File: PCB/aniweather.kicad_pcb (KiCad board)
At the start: 2 copper layers, 55 x 75 mm, 26 parts, among them SW1 SW_DIP_x01, SW2 SW_Push, U5 TPS63001

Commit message: Reroute board
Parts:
- added R4: 100k, Resistor_THT:R_Axial_DIN0207_L6.3mm_D2.5mm_P10.16mm_Horizontal, F.Cu at (139.3, 136.2)
- added SW3: SW_Push, Button_Switch_THT:SW_PUSH_6mm, F.Cu at (122.0, 136.2)
- moved G1 71.2 mm to (69.2, 98.7)
- moved G2 71.2 mm to (69.2, 98.7)
- moved C1 6.21 mm to (122.8, 125.9), turned to 0 degrees
- moved SW2 0.45 mm to (158.4, 129.7)
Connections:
- U1 pad 10: SD_MISO -> MISO
- U1 pad 11: SD_SCK -> SCK
- U1 pad 5: SDA -> MOSI
- U1 pad 9: SD_MOSI -> MOSI
- U2 pad 0: SDA -> Net-(U2-A0)
- U2 pad 10: SD_CS -> CS_LCD
- U2 pad 2: RESET -> MISO
- U2 pad 3: CS_LCD -> RESET
- U2 pad 4: SCK -> unconnected-(U2-A4-Pad4)
- U2 pad 6: SD_SCK -> SCK
- U2 pad 7: SD_MISO -> MOSI
- U2 pad 8: SD_MOSI -> SD_CS
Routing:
- net MOSI: track 0.00 -> 62.5 mm
- net MISO: track 0.00 -> 46.1 mm
- net SCK: track 15.4 -> 60.4 mm
- net Net-(U2-A0): track 0.00 -> 41.7 mm
- net SD_MISO: track 25.3 -> 0.00 mm
- net SD_SCK: track 25.3 -> 0.00 mm
- net SD_MOSI: track 25.3 -> 0.00 mm
- net CS_LCD: track 12.9 -> 36.2 mm
- net SDA: track 14.7 -> 0.00 mm
- net +3.3V: track 89.2 -> 101.8 mm
- net GND: track 23.3 -> 19.9 mm, vias 72 -> 71
- net RESET: track 12.9 -> 11.1 mm
- net SD_CS: track 25.8 -> 26.7 mm

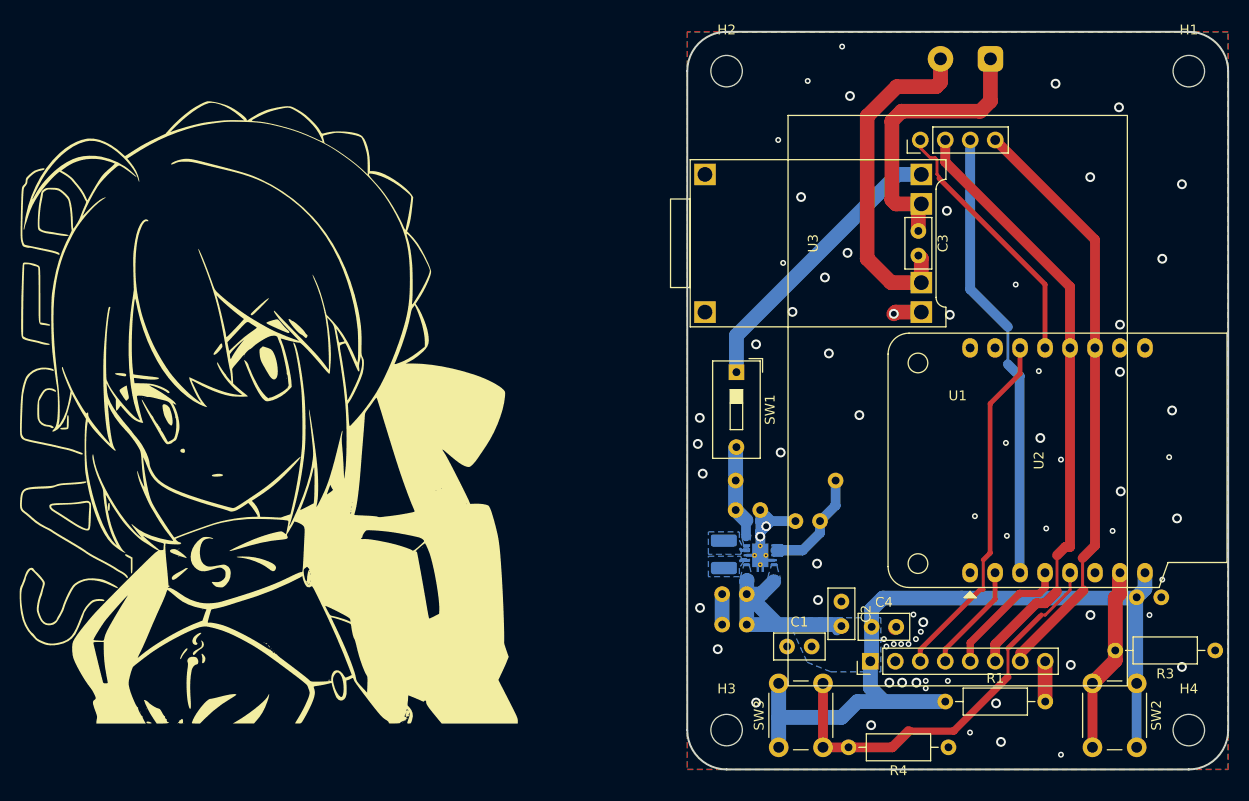
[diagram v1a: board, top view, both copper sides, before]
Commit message: Round corner cases and button holes
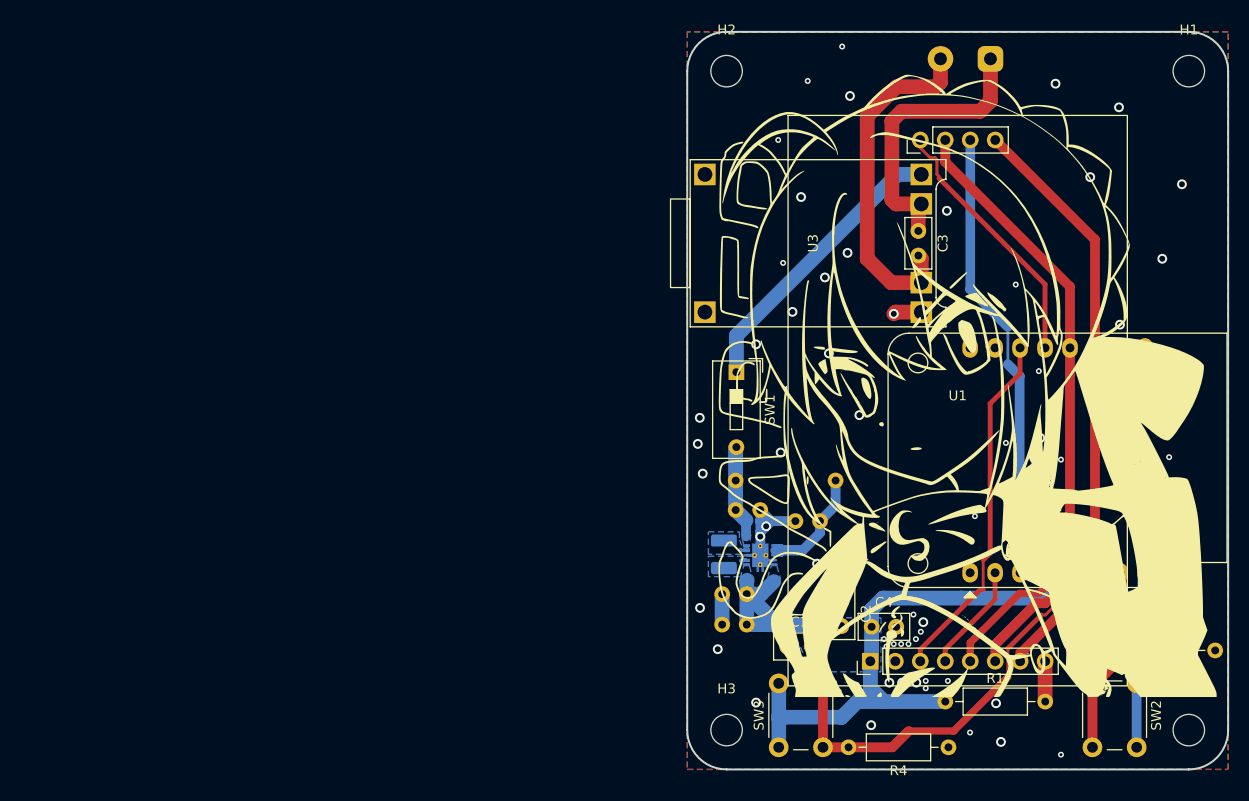
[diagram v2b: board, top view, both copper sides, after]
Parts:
- moved G1 71.1 mm to (140.3, 96.0)
- moved G2 71.1 mm to (140.3, 96.0)
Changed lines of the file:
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@@
 	(footprint "LOGO"
 		(layer "F.Cu")
-		(at 69.2 98.725)
+		(at 140.25115 96.027339)
 		(property "Reference" "G2"
 			(at 0 0 0)
@@
 		)
 		(property "Footprint" ""
-			(at 0 0 90)
+			(at 0 0 -90)
 			(layer "F.Fab")
 			(hide yes)
@@
 		(tags "C Disc series Radial pin pitch 2.50mm  diameter 5mm width 2.5mm Capacitor")
 		(property "Reference" "C1"
-			(at 1.25 -2.5 360)
+			(at 1.25 -2.5 0)
 			(layer "F.SilkS")
 			(effects
@@
 		)
 		(property "Value" "Tiny"
-			(at 1.25 2.5 360)
+			(at 1.25 2.5 0)
 			(layer "F.Fab")
 			(effects
@@
 		)
 		(property "Footprint" ""
-			(at 0 0 360)
+			(at 0 0 0)
 			(layer "F.Fab")
 			(hide yes)
@@
 		)
 		(fp_text user "${REFERENCE}"
-			(at 1.25 0 360)
+			(at 1.25 0 0)
 			(layer "F.Fab")
 			(effects
@@
 		(tags "Resistor Axial_DIN0207 series Axial Horizontal pin pitch 10.16mm 0.25W = 1/4W length 6.3mm diameter 2.5mm")
 		(property "Reference" "R4"
-			(at 5.08 -2.37 360)
+			(at 5.08 -2.37 0)
 			(layer "F.SilkS")
 			(effects
@@
 		)
 		(property "Value" "100k"
-			(at 5.25 2.55 360)
+			(at 5.25 2.55 0)
 			(layer "F.Fab")
 			(effects
@@
 		)
 		(property "Footprint" ""
-			(at 0 0 360)
+			(at 0 0 180)
 			(layer "F.Fab")
 			(hide yes)
@@
 		)
 		(fp_text user "${REFERENCE}"
-			(at 5.08 0 360)
+			(at 5.08 0 0)
 			(layer "F.Fab")
 			(effects
@@
 	(footprint "LOGO"
 		(layer "B.Cu")
-		(at 69.2 98.725 180)
+		(at 140.25115 96.027339 180)
 		(property "Reference" "G1"
 			(at 0 0 0)

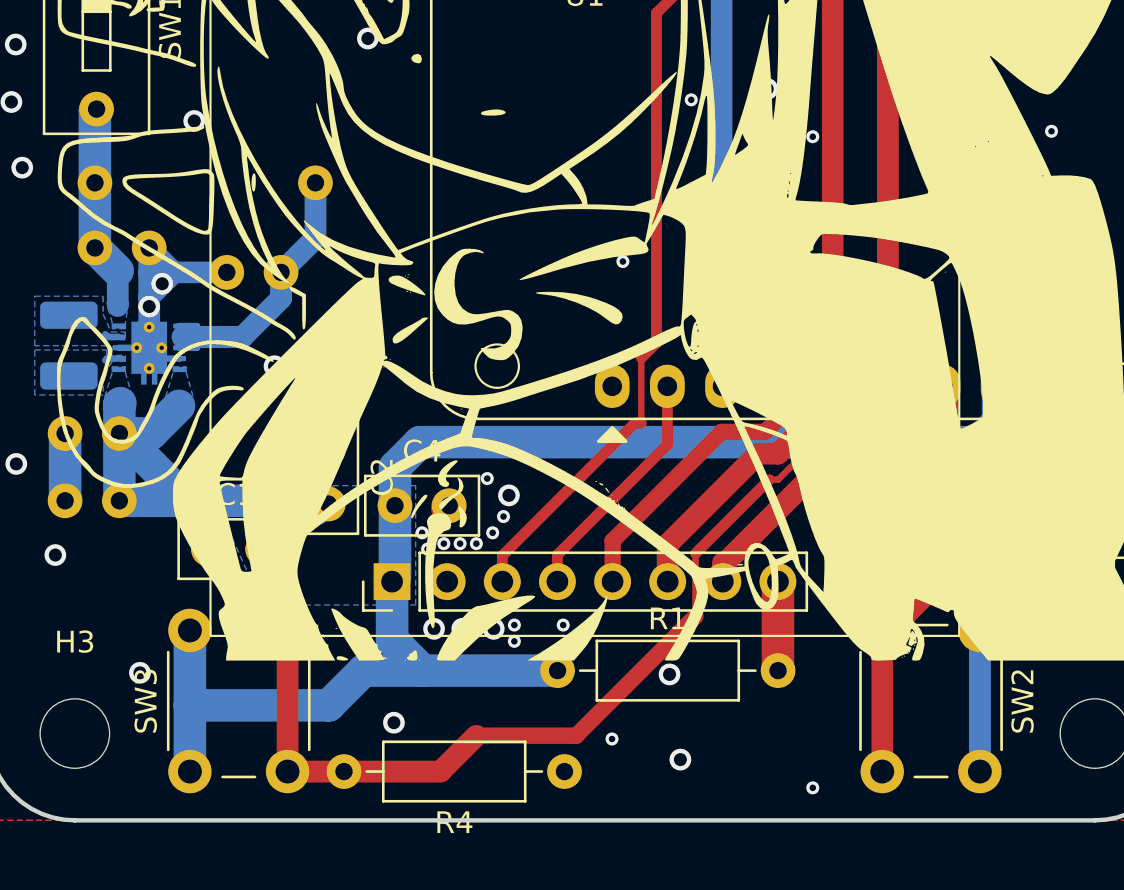
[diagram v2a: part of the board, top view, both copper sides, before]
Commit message: Revisions for PCB and start of the firmware
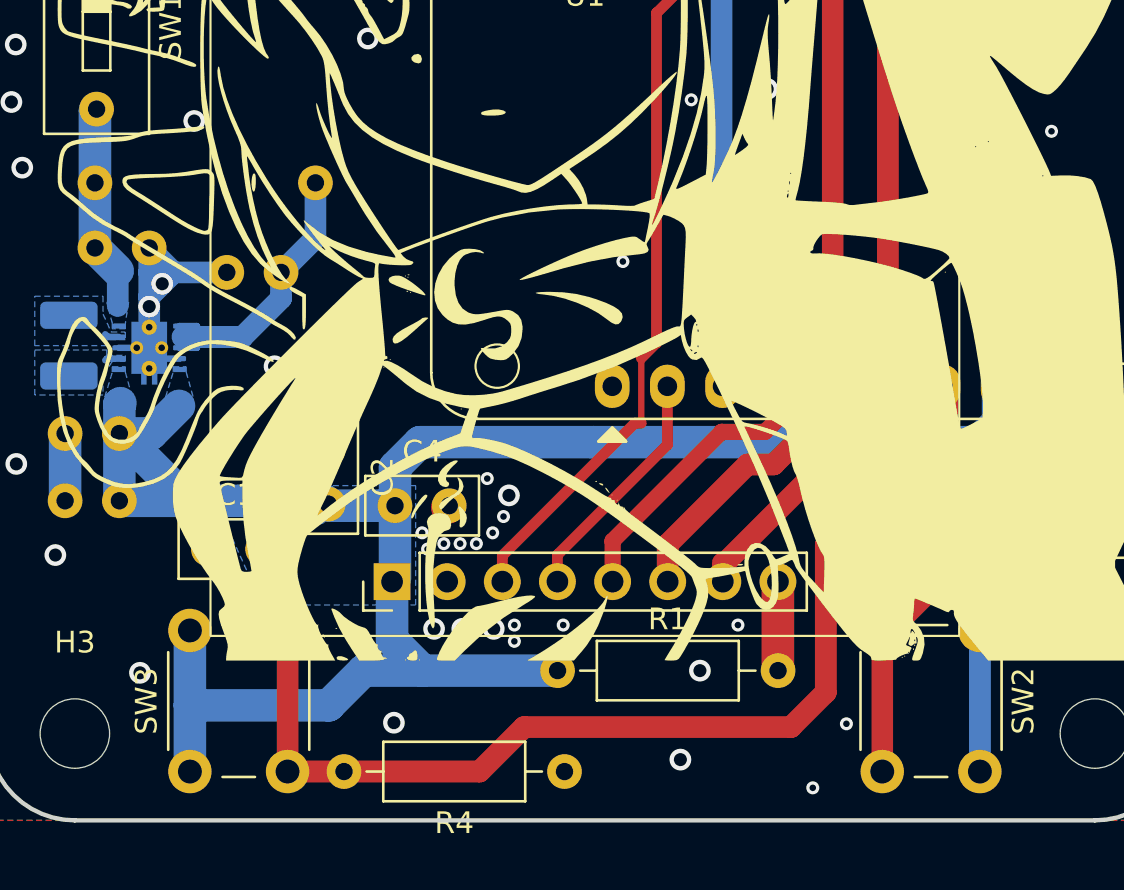
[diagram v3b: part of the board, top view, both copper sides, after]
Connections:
- R4 pad 2: Net-(U2-A0) -> Net-(U2-A4)
- SW3 pad 2: Net-(U2-A0) -> Net-(U2-A4)
- U2 pad 0: Net-(U2-A0) -> unconnected-(U2-A0-Pad0)
- U2 pad 4: unconnected-(U2-A4-Pad4) -> Net-(U2-A4)
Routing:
- net Net-(U2-A4): track 0.00 -> 48.1 mm
- net Net-(U2-A0): track 41.7 -> 0.00 mm
- net +3.3V: track 101.8 -> 105.0 mm, vias 0 -> 1
- net GND: vias 71 -> 70

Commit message: Final revision
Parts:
- added JP1: Jumper_2_Bridged, Resistor_THT:R_Axial_DIN0207_L6.3mm_D2.5mm_P15.24mm_Horizontal, F.Cu at (141.0, 92.4)
- added R5: 10k, Resistor_THT:R_Axial_DIN0207_L6.3mm_D2.5mm_P10.16mm_Horizontal, F.Cu at (146.2, 86.3)
- added R6: 10k, Resistor_THT:R_Axial_DIN0207_L6.3mm_D2.5mm_P10.16mm_Horizontal, F.Cu at (147.2, 89.4)
- added R7: 10k, Resistor_THT:R_Axial_DIN0207_L6.3mm_D2.5mm_P10.16mm_Horizontal, F.Cu at (141.4, 83.3)
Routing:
- net +3.3V: track 105.0 -> 146.4 mm, vias 1 -> 0
- net CS_LCD: track 36.2 -> 43.0 mm
- net GND: track 19.9 -> 17.0 mm, vias 70 -> 53
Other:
- board text added: "${TITLE} Rev ${REVISION} ${CURRENT_DATE}"

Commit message: PCB revision
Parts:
- JP1: value Jumper_2_Bridged -> Jumper_2_Open; footprint Resistor_THT:R_Axial_DIN0207_L6.3mm_D2.5mm_P15.24mm_Horizontal -> Jumper:SolderJumper-2_P1.3mm_Open_Pad1.0x1.5mm; moved to B.Cu
- moved JP1 25.1 mm to (117.7, 101.7), turned to 90 degrees
- moved R7 0.08 mm to (141.4, 83.3)
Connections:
- C6 pad 1: Net-(U5-VIN) -> Net-(JP1-A)
- JP1 pad 1: GND -> Net-(JP1-A)
- JP1 pad 2: GND -> Net-(JP1-B)
- R2 pad 2: Net-(U5-VIN) -> Net-(JP1-A)
- SW1 pad 1: Net-(U3-OUT+) -> Net-(JP1-B)
- SW1 pad 2: Net-(U5-VIN) -> Net-(JP1-A)
- U3 pad 2: Net-(U3-OUT+) -> Net-(JP1-B)
- U5 pad 5: Net-(U5-VIN) -> Net-(JP1-A)
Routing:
- net Net-(JP1-B): track 0.00 -> 33.4 mm
- net Net-(U3-OUT+): track 29.3 -> 0.00 mm
- net Net-(JP1-A): track 0.00 -> 12.6 mm
- net Net-(U5-VIN): track 9.54 -> 0.00 mm
- net +3.3V: track 146.4 -> 138.6 mm
- net MISO: track 46.1 -> 51.0 mm
- net GND: track 17.0 -> 18.2 mm, vias 53 -> 49
- net CS_LCD: vias 0 -> 1
- added copper zone on B.Cu, net Net-(JP1-A)
- removed copper zone on B.Cu, net Net-(U5-VIN)

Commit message: I hope this is the final revision
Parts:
- added JP2: Jumper_2_Open, Jumper:SolderJumper-2_P1.3mm_Open_Pad1.0x1.5mm, B.Cu at (123.8, 70.5)
- added JP3: Jumper_2_Open, Jumper:SolderJumper-2_P1.3mm_Open_Pad1.0x1.5mm, F.Cu at (116.8, 94.7)
- added JP4: Jumper_2_Open, Jumper:SolderJumper-2_P1.3mm_Open_Pad1.0x1.5mm, B.Cu at (132.8, 74.8)
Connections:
- U2 pad 14: unconnected-(U2-VBUS-Pad14) -> VBUS
- U3 pad 4: unconnected-(U3-IN+-Pad4) -> Net-(JP2-A)
- U3 pad 5: unconnected-(U3-IN--Pad5) -> Net-(JP3-B)
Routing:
- net VBUS: track 0.00 -> 58.9 mm
- net Net-(JP2-A): track 0.00 -> 13.5 mm
- net Net-(JP3-B): track 0.00 -> 3.57 mm
- net Net-(JP1-B): track 33.4 -> 35.6 mm
- net MISO: track 51.0 -> 50.0 mm
- net GND: vias 49 -> 50

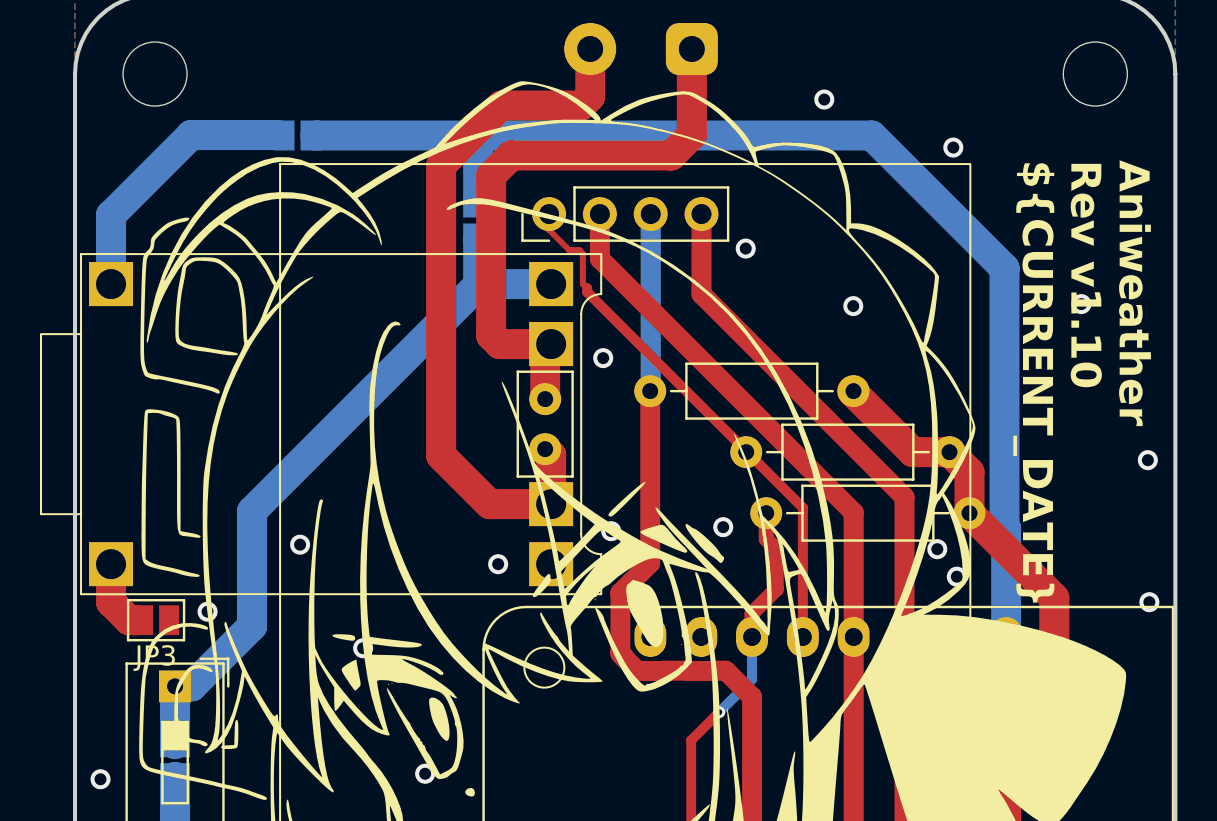
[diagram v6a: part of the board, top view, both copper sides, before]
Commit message: Add diode
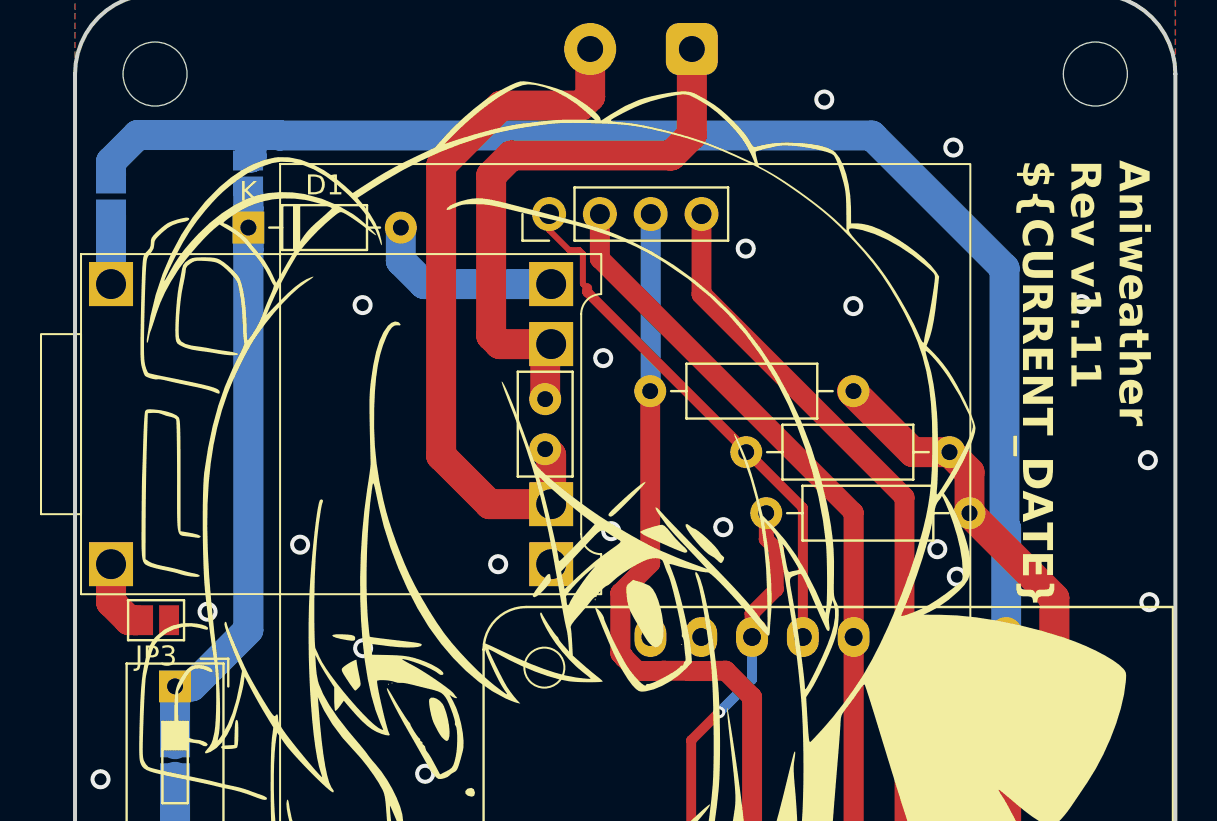
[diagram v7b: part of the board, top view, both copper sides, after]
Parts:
- added D1: D, Diode_THT:D_DO-35_SOD27_P7.62mm_Horizontal, F.Cu at (121.4, 75.1)
- moved JP4 11.7 mm to (121.3, 72.4)
- moved JP2 9.81 mm to (114.5, 73.5), turned to 90 degrees
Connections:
- JP1 pad 2: Net-(JP1-B) -> Net-(D1-K)
- JP4 pad 2: Net-(JP1-B) -> Net-(D1-K)
- SW1 pad 1: Net-(JP1-B) -> Net-(D1-K)
- U3 pad 2: Net-(JP1-B) -> Net-(D1-A)
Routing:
- net Net-(JP1-B): track 35.6 -> 0.00 mm
- net Net-(D1-K): track 0.00 -> 31.6 mm
- net Net-(JP2-A): track 13.5 -> 3.45 mm
- net Net-(D1-A): track 0.00 -> 9.66 mm
- net VBUS: track 58.9 -> 68.4 mm
- net GND: vias 50 -> 51
